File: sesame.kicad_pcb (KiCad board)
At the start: 2 copper layers, 344.4 x 130.9 mm, 166 parts, among them U1 ATmega32A-PU

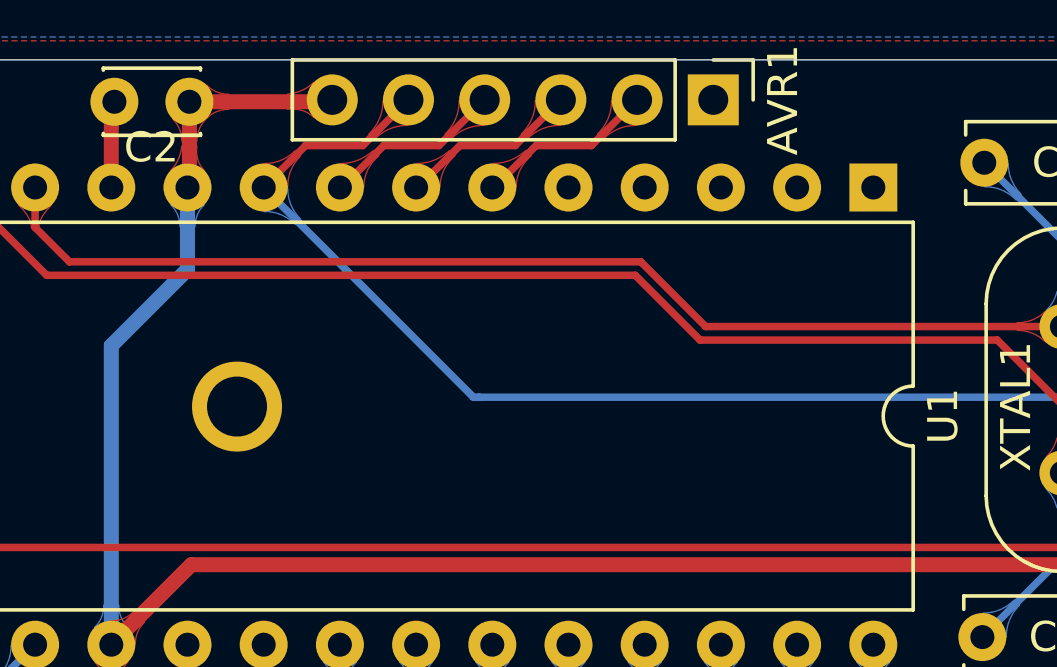
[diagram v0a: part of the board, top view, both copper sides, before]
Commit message: added rgb header
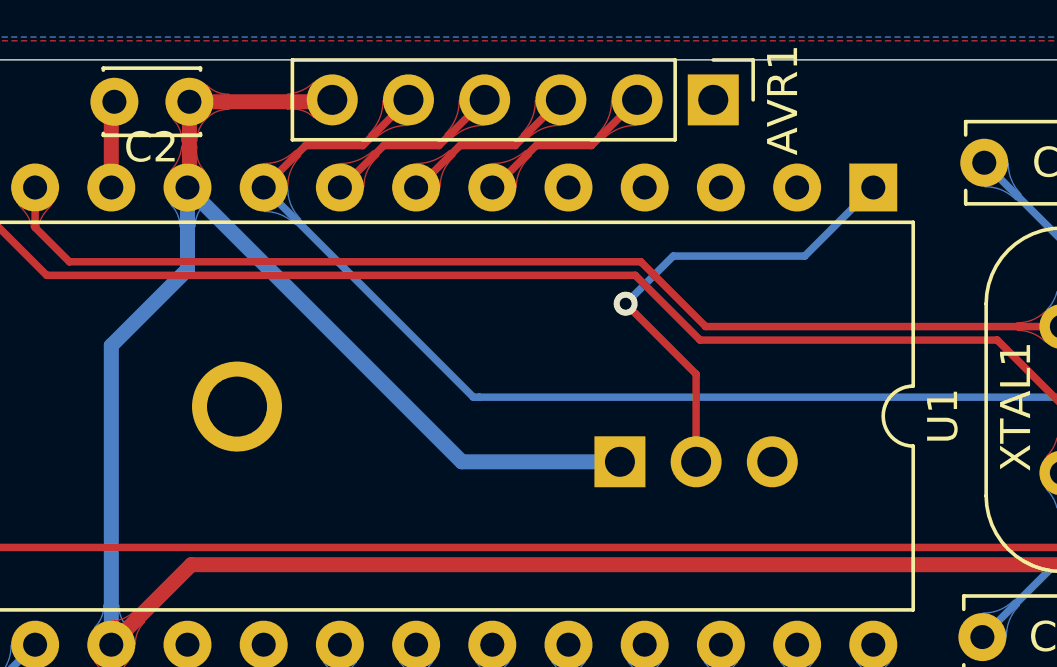
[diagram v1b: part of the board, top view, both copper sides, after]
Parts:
- added J1: Conn_01x03_Female, Connector_PinHeader_2.54mm:PinHeader_1x03_P2.54mm_Vertical, B.Cu at (224.6, 78.9)
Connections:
- U1 pad 1: Net-(U1-Pad1) -> RGB
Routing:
- net +5V: track 145.7 -> 163.9 mm
- net RGB: track 0.00 -> 16.1 mm, vias 0 -> 1
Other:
- board text added: "5V"
- board text added: "D"
- board text added: "G"

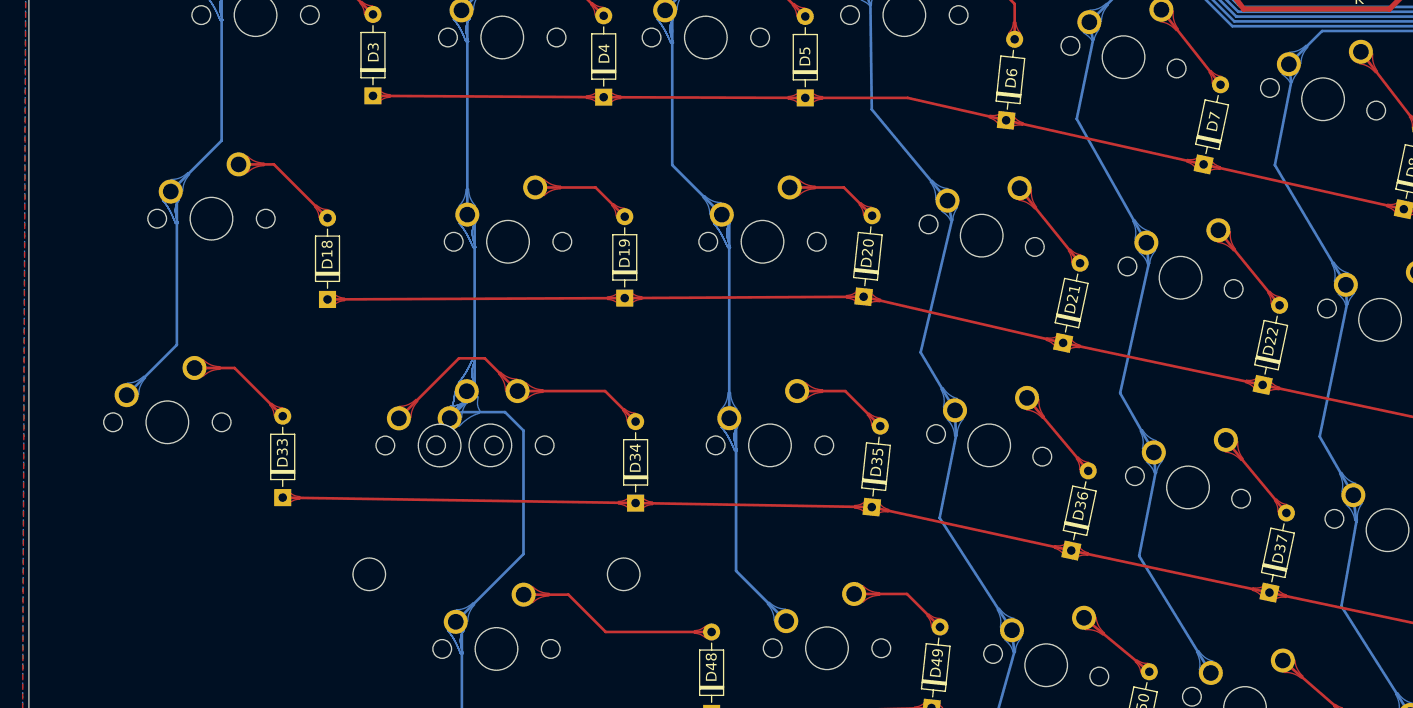
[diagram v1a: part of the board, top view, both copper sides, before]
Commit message: add
-Double check implementation of Ws2812b(ex. caps for each led), (resistor between dataline and MCU pin)
-Add more more RGB LEDS to the schematic,  generate netlist
- OPen pcb view, read netlist, place the LEDs. Make sure on correct side. Then route traces
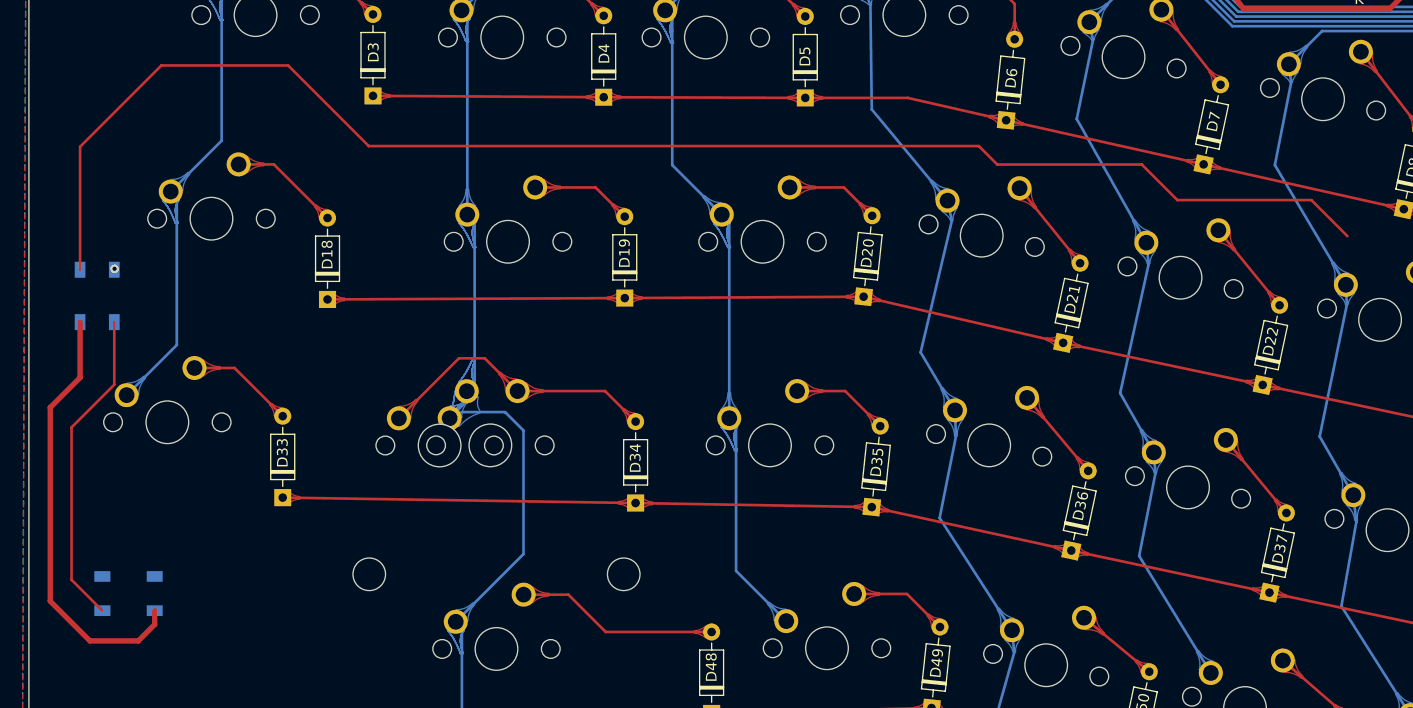
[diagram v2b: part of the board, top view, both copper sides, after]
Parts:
- added D69: WS2812B, LED_SMD:LED_WS2812B_PLCC4_5.0x5.0mm_P3.2mm, B.Cu at (47.0, 113.5)
- added D70: WS2812B, LED_SMD:LED_WS2812B_PLCC4_5.0x5.0mm_P3.2mm, B.Cu at (50.0, 141.3)
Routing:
- net RGB: track 16.1 -> 156.0 mm
- net +5V: track 163.9 -> 204.4 mm
- net Net-(D69-Pad2): track 0.00 -> 29.9 mm, vias 0 -> 1
